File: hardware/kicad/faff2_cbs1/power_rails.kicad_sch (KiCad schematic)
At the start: 60 parts, among them U301 LMR33630, U302 TPS7A20, U303 TPS7A20, U304 LMR33630

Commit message: review r1 batch 2: power_rails - LMR51610 pre-regulator, dual TPs, flow fixes
The captain's second review batch, all six points, on power_rails.

  1  TP301 and TP305 deleted - test coverage off both PSU feedback nodes, and
     that same edit leaves U301's 4-way FB junction a plain 3-way tee
  2  every regulator output gets an Amodo TestPointDual (probe pad + ground
     clip), hung below its rail on a stub so the pads clear the wire they tap
  3  R305/R306/R307/R312 laid horizontal, so each rail runs one way and steps
     down once instead of stepping through its own link
  4  U301 -> LMR51610XFDBVR, the buck ARIA_EITSYS_CBs_1 uses
  5  FB301 laid horizontal, in line on the +3V3 rail
  6  D303 stood vertical, anode up out of R314

Point 4 is the authorised design change and it moves the netlist: 409 -> 405
components, 253 -> 251 nets, ERC still 0 errors / 0 warnings at severity-all.
Every node-set change is tabulated and accounted for in the decisions file.

Re-derived from TI SLUSEY1B (committed as datasheets/LMR51610.pdf), whose own
worked example is a 24 V -> 5 V 400 kHz design:
  - VFB is 0.8 V not 1.0 V, so R304 22.1k -> 16.9k: 100k/16.9k = 5.534 V, still
    inside the TPS7A20's 6.0 V input maximum with 0.53 V of dropout headroom
  - L301 15uH -> 33uH (SRN6045TA, 1.8 Arms / 2.5 Asat), KIND = 0.32
  - EN divider unchanged - VEN(R) 1.227 V matches the LMR33630's, so the 16.2 V
    UVLO stands
  - C304 and the thermal-pad ground go: the part has neither pin
  - no PG pin either, so R315 goes and RAIL_PGOOD is the +3V3 buck's PG alone

U304 stays LMR33630: its rail's 1.1 A budget exceeds the LMR51610's 1 A rating.
Both 5 V LDOs stay TPS7A20: the reference design's ADPL42005 is 32 uVrms against
the TPS7A20's 7 uVrms, on the rail carrying REQ-FF-04's noise budget. Both kept
parts are written up with their reasoning, and the LDO one is raised for the
captain to overrule.

Also fixed in passing: R314's right-justified fields put "330R" against C324's
GND label - a 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
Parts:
- removed C304: 1uF, Amodo:C_0603_1608Metric, symbol Amodo_Capacitors:CAP_MLCC_1uF_0603_10%_16V
- removed L301: 15uH, Amodo:L_Bourns_SRR1210, symbol Amodo_Inductors:IND_SMD_15uH_5.3A
- removed R304: 22k1, Amodo:R_0603_1608Metric, symbol Amodo_Resistors:RES_TNF_22.1k_0603_0.1%
- removed R315: 1k, Amodo:R_0603_1608Metric, symbol Amodo_Resistors:RES_TF_1k_0603
- removed TP301, TP305: FB, Amodo:TestPoint_Pad_D1.0mm, symbol Amodo_Connectors:TestPoint
- removed TP302: +5V5, Amodo:KeystoneMiniatureTestLoop, symbol Amodo_Connectors:TestPointHook
- removed TP303: +5V, Amodo:KeystoneMiniatureTestLoop, symbol Amodo_Connectors:TestPointHook
- removed TP304: +5VA, Amodo:KeystoneMiniatureTestLoop, symbol Amodo_Connectors:TestPointHook
- removed TP306: +3V3, Amodo:KeystoneMiniatureTestLoop, symbol Amodo_Connectors:TestPointHook
- removed TP307: +3V3A, Amodo:KeystoneMiniatureTestLoop, symbol Amodo_Connectors:TestPointHook
- removed U301: LMR33630, Amodo:PowerPAD SOIC-8 HSOIC (8), symbol Amodo_Power_ICs:LMR33630
- added L301: 33uH, Amodo:L_Bourns_SRN6045TA_6x6mm, symbol Amodo_Inductors:IND_SMD_33uH
- added R304: 16k9, Amodo:R_0603_1608Metric, symbol Amodo_Resistors:RES_TNF_16.9k_0603_0.1%
- added TP302: +5V5, Amodo:TestPoint_Dual_D1.5mm_H1.0mm, symbol Amodo_Connectors:TestPointDual
- added TP303: +5V, Amodo:TestPoint_Dual_D1.5mm_H1.0mm, symbol Amodo_Connectors:TestPointDual
- added TP304: +5VA, Amodo:TestPoint_Dual_D1.5mm_H1.0mm, symbol Amodo_Connectors:TestPointDual
- added TP306: +3V3, Amodo:TestPoint_Dual_D1.5mm_H1.0mm, symbol Amodo_Connectors:TestPointDual
- added TP307: +3V3A, Amodo:TestPoint_Dual_D1.5mm_H1.0mm, symbol Amodo_Connectors:TestPointDual
- added U301: LMR51610, Amodo:SOT23-6, symbol Amodo_Power_ICs:LMR51610XFDBVR
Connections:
- net +3V3: now also TP306.1
- net +3V3A: now also TP307.1
- net +5V: now also TP303.1
- net +5V5: now also TP302.1
- net +5VA: now also TP304.1
- net GND: now also R304.2, TP302.2, TP303.2, TP304.2, TP306.2, TP307.2, U301.2 (GND)
- net V24_LOGIC: now also U301.5 (VIN)
- net at C306.1, C307.1, C308.1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: now also L301.2
- net at R303.2: now also R304.1, U301.3 (FB)
- net at C305.2: now also L301.1, U301.6 (SW)
- net at R301.2, R302.1: now also U301.4 (EN)
- net at C305.1: now also U301.1 (CB)
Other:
- note added: "A. PRE-REGULATOR V24_LOGIC -> 5.5 V (LMR51610, 400 kHz)"
- note added: "BLOCK: power_rails - rail set and topology; answers OQ-02 and OQ-07 RAILS +5V5 LMR51610 buck from V24_LOGIC. Pre-regulator only, local to this sheet. +5V TPS7A20 LDO from +5V5. IKP11 read head (<65 mA plus RS-422 drive) and spare. +5VA TPS7A20 LDO from +5V5. ADS1235 / ADS1120 AVDD and the AFE 5 V excitation and reference chain, which lives in loadcell_afe - take it from +5VA, not +5V. +3V3 LMR336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"
- note added: "PER RAIL (docs/TEST_PLAN.md 3.1) one 0R link that is BOTH the isolation link and the current-measurement break, a test point downstream of it, on a dual pad so a scope ground clips beside the probe. No test point sits on a feedback node: R305 +5V5, R306 +5V, R307 +5VA, R312 +3V3, FB301 +3V3A. Per-CONSUMER links are not here: every block takes the same global rail net, so per-block breaks would ne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"
- note removed: "A. PRE-REGULATOR V24_LOGIC -> 5.5 V (LMR33630, 400 kHz)"
- note removed: "BLOCK: power_rails - rail set and topology; answers OQ-02 and OQ-07 RAILS +5V5 LMR33630 buck from V24_LOGIC. Pre-regulator only, local to this sheet. +5V TPS7A20 LDO from +5V5. IKP11 read head (<65 mA plus RS-422 drive) and spare. +5VA TPS7A20 LDO from +5V5. ADS1235 / ADS1120 AVDD and the AFE 5 V excitation and reference chain, which lives in loadcell_afe - take it from +5VA, not +5V. +3V3 LMR336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"
- note removed: "PER RAIL (docs/TEST_PLAN.md 3.1) one 0R link that is BOTH the isolation link and the current-measurement break, a test point downstream of it, and a test point on each feedback node: R305 +5V5, R306 +5V, R307 +5VA, R312 +3V3, FB301 +3V3A. Per-CONSUMER links are not here: every block takes the same global rail net, so per-block breaks would need per-block rail names and would break the frozen bloc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"
- moved on the sheet: D303, FB301, R305, R306, R307, R312

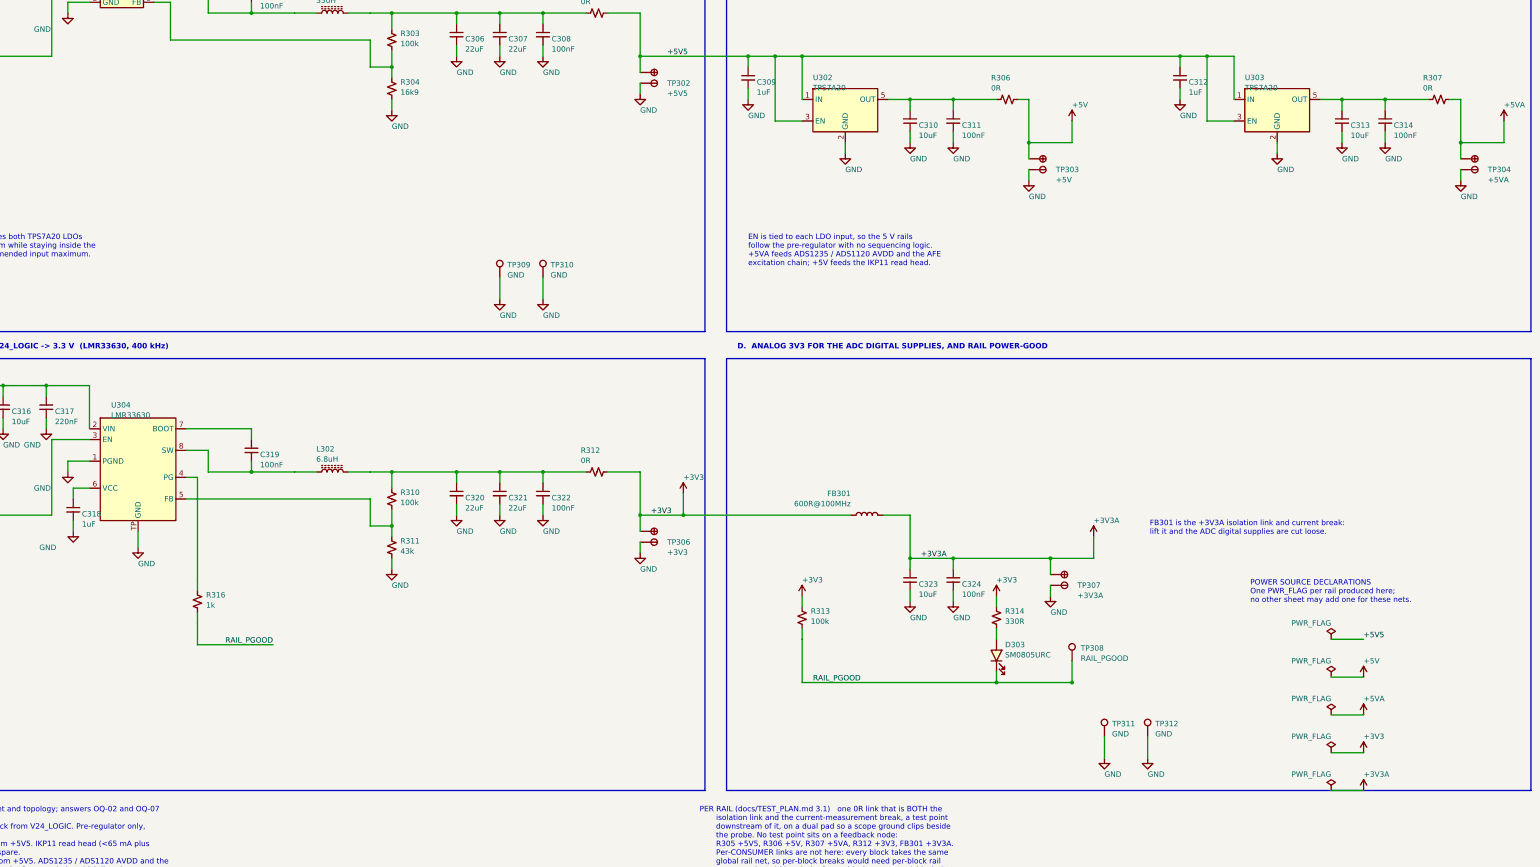
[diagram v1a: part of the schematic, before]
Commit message: review r1 final sweep: power labels, TP silkscreen names, text overlaps
The captain's design-wide pass, run once the per-sheet batches had landed.
Presentation only: ERC 0 errors / 0 warnings at severity-all, 404 components,
251 nets, and every per-net node set identical to the pre-sweep export.

  power labels   92 rail names were hidden on loadcell_afe, motor_drive and
                 temp_sense - all 285 power symbols now read, placed to the
                 house pattern (GND below the symbol, rail arrows above)
  test points    66 of 83 still carried the library default "TestPoint". All
                 83 now name what they measure, from the net they actually
                 land on in the netlist; longest is 5 characters
  text overlap   16 collisions cleared design-wide, four of them sub-millimetre
                 ones the bundled checker passes because it under-measures text
  GND upside down  none - 0 of 285 power symbols is rotated or mirrored
  graphic/wire   one: power_rails block D's bottom border lay along the last
                 PWR_FLAG's wire; the flag column moved up 2.54

The overlap checker turns out to have three separable blind spots, each settled
here by measuring a render rather than by reading the format: it grows every
text field rightward regardless of justify/mirror/180-rotation, so its box is a
mirror image of the truth for those and it both invents and misses collisions;
it measures text at ~1.06 mm per character where the real advance is ~1.19; and
it reflects a rotated symbol's body about the origin. tools/sch_geom.py models
all three correctly and the design is clean under it design-wide. Two of that
model's own rules - notes growing up from their anchor, and labels taking no
180-degree justify flip - were bugs of mine that the checker caught first. The
render is what settles it; neither tool is authoritative alone.

Placement is searched rather than guessed: 177 newly visible fields are tried
against every wire, block border, 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
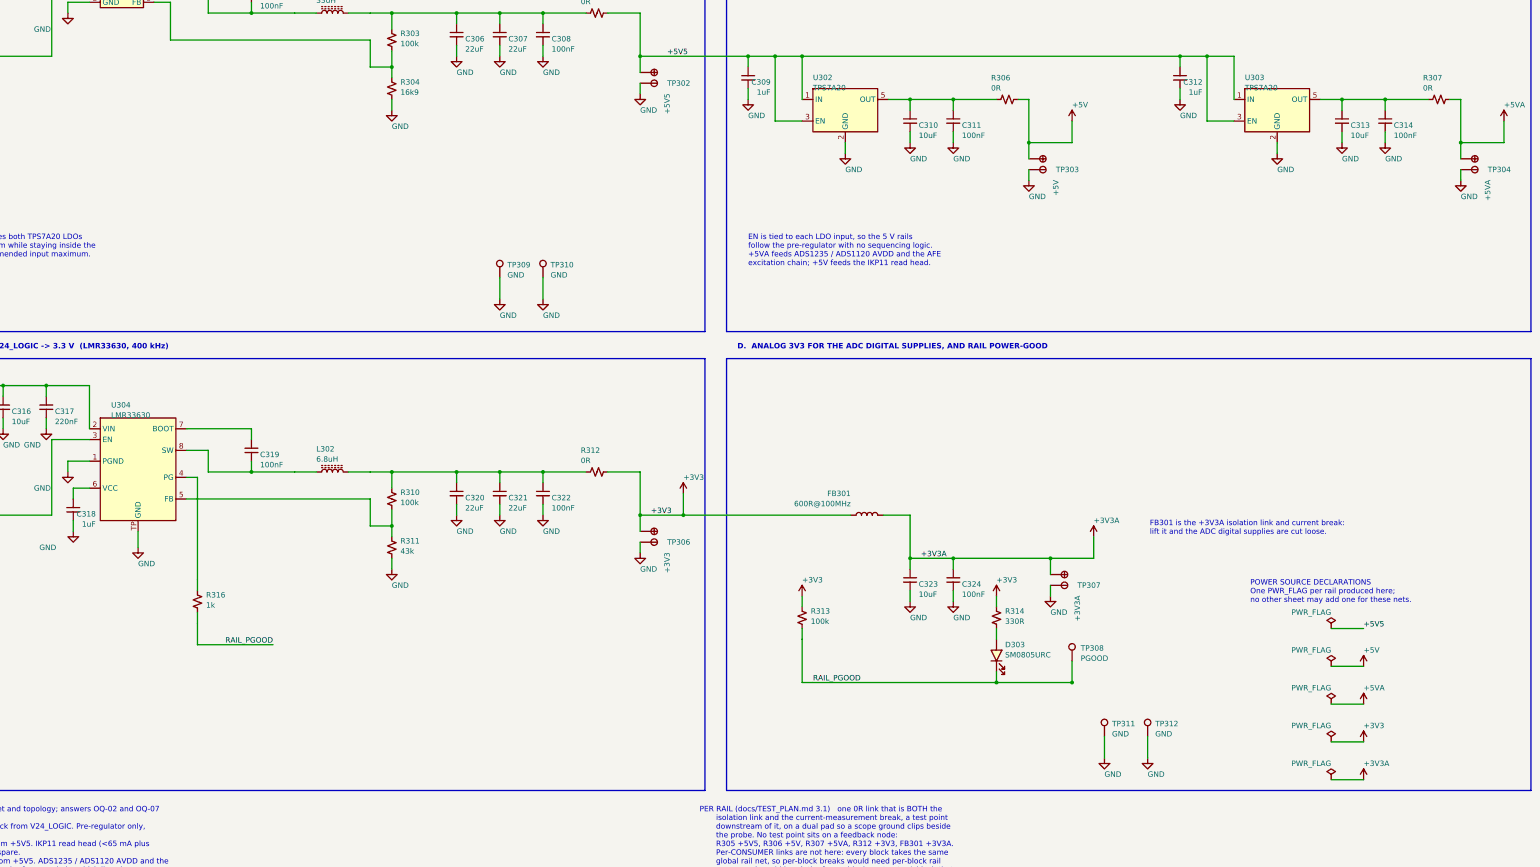
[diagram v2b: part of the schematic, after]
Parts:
- TP308: value RAIL_PGOOD -> PGOOD

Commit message: review r2 item 1: U301 back to the LMR33630
The captain overruled the reference-part swap for U301 only. Reverted the buck,
R304 (16.9k -> 22.1k), L301 (33uH -> 15uH), and the three parts the LMR51610 had
no pins for: C304 on VCC, the thermal-pad ground, and R315 in the PG leg.
RAIL_PGOOD is the wired-AND of both converters again.

The seven symbols are restored verbatim from 48a5f4f rather than rebuilt, so they
keep their original uuids, and the sheet notes revert with them.

Everything else round 1 did to power_rails stands, because none of it depended on
which buck was fitted: the five dual test points, the horizontal 0R links and
ferrite, the vertical power LED, and no test point on either feedback node -
TP301 stays deleted.

ERC 0 errors / 0 warnings at severity-all; 404 -> 406 components and 251 -> 253
nets, exactly C304, R315 and the VCC and PG nets coming back.

Co-Authored-By: Claude Opus 5 <noreply@anthropic.com>
Claude-Session: https://claude.ai/code/session_01PFWfwT8RZc8Zqn8vgZxV8j
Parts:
- removed L301: 33uH, Amodo:L_Bourns_SRN6045TA_6x6mm, symbol Amodo_Inductors:IND_SMD_33uH
- removed R304: 16k9, Amodo:R_0603_1608Metric, symbol Amodo_Resistors:RES_TNF_16.9k_0603_0.1%
- removed U301: LMR51610, Amodo:SOT23-6, symbol Amodo_Power_ICs:LMR51610XFDBVR
- added C304: 1uF, Amodo:C_0603_1608Metric, symbol Amodo_Capacitors:CAP_MLCC_1uF_0603_10%_16V
- added L301: 15uH, Amodo:L_Bourns_SRR1210, symbol Amodo_Inductors:IND_SMD_15uH_5.3A
- added R304: 22k1, Amodo:R_0603_1608Metric, symbol Amodo_Resistors:RES_TNF_22.1k_0603_0.1%
- added R315: 1k, Amodo:R_0603_1608Metric, symbol Amodo_Resistors:RES_TF_1k_0603
- added U301: LMR33630, Amodo:PowerPAD SOIC-8 HSOIC (8), symbol Amodo_Power_ICs:LMR33630
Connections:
- net GND: now also C304.2, R304.2, U301.1 (PGND), U301.TP (GND)
- net RAIL_PGOOD: now also R315.2
- net V24_LOGIC: now also U301.2 (VIN)
- net at C306.1, C307.1, C308.1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: now also L301.2
- net at C305.1: now also U301.7 (BOOT)
- net at R303.2: now also R304.1, U301.5 (FB)
- net at R301.2, R302.1: now also U301.3 (EN)
- net at C305.2: now also L301.1, U301.8 (SW)
- new net: C304.1, U301.6 (VCC)
- new net: R315.1, U301.4 (PG)
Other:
- note added: "A. PRE-REGULATOR V24_LOGIC -> 5.5 V (LMR33630, 400 kHz)"
- note added: "BLOCK: power_rails - rail set and topology; answers OQ-02 and OQ-07 RAILS +5V5 LMR33630 buck from V24_LOGIC. Pre-regulator only, local to this sheet. +5V TPS7A20 LDO from +5V5. IKP11 read head (<65 mA plus RS-422 drive) and spare. +5VA TPS7A20 LDO from +5V5. ADS1235 / ADS1120 AVDD and the AFE 5 V excitation and reference chain, which lives in loadcell_afe - take it from +5VA, not +5V. +3V3 LMR336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"
- note removed: "A. PRE-REGULATOR V24_LOGIC -> 5.5 V (LMR51610, 400 kHz)"
- note removed: "BLOCK: power_rails - rail set and topology; answers OQ-02 and OQ-07 RAILS +5V5 LMR51610 buck from V24_LOGIC. Pre-regulator only, local to this sheet. +5V TPS7A20 LDO from +5V5. IKP11 read head (<65 mA plus RS-422 drive) and spare. +5VA TPS7A20 LDO from +5V5. ADS1235 / ADS1120 AVDD and the AFE 5 V excitation and reference chain, which lives in loadcell_afe - take it from +5VA, not +5V. +3V3 LMR336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"

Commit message: review r2 item 2: power_rails PWR_FLAGs moved to their regulators
They sat in a column of their own in block D, each flag hung off a duplicate
power symbol that existed only to give it a net. Each now taps the rail it
declares, on the load side of that rail's 0R link - before the link is a
different net, so a flag there would declare the wrong thing.

#PWR346/348/350/352 went with the column: every one of those rails already
carries a power symbol at its output, so the duplicates declared nothing new.
Node sets are identical across the change, which is the proof. #FLG301 stays -
V24_LOGIC arrives at the sheet rather than being made on it, and its flag is
already beside U301.

Also fixed, caught in the render rather than by any tool: TP302/303/304/306/307
are TestPointDual at 270 degrees, and round 1's placement pass rewrote their
Value with angle 0 instead of the 90 that compensates the rotation, so the
silkscreen names were reading vertically. The sweep script now preserves a
field's angle when it moves it, so it cannot recur.

ERC 0 errors / 0 warnings at severity-all; 406 components, 253 nets, node sets
unchanged.

Co-Authored-By: Claude Opus 5 <noreply@anthropic.com>
Claude-Session: https://claude.ai/code/session_01PFWfwT8RZc8Zqn8vgZxV8j
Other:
- note added: "POWER SOURCE DECLARATIONS One PWR_FLAG per rail produced here, at the regulator that makes it, on the load side of that rail's 0R link. No other sheet may add one for these nets."
- note removed: "POWER SOURCE DECLARATIONS One PWR_FLAG per rail produced here; no other sheet may add one for these nets."
